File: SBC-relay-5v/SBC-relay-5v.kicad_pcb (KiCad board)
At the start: 2 copper layers, 85 x 56 mm, 52 parts, among them J1 USB_B_Micro, J2 PWR_IN, J3 USB_A_Stacked, J4 USB_A_Stacked, J5 USB_A, J6 USB_A, K1 SANYOU_SRD_Form_A, K2 SANYOU_SRD_Form_A, K3 SANYOU_SRD_Form_A, K4 SANYOU_SRD_Form_A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

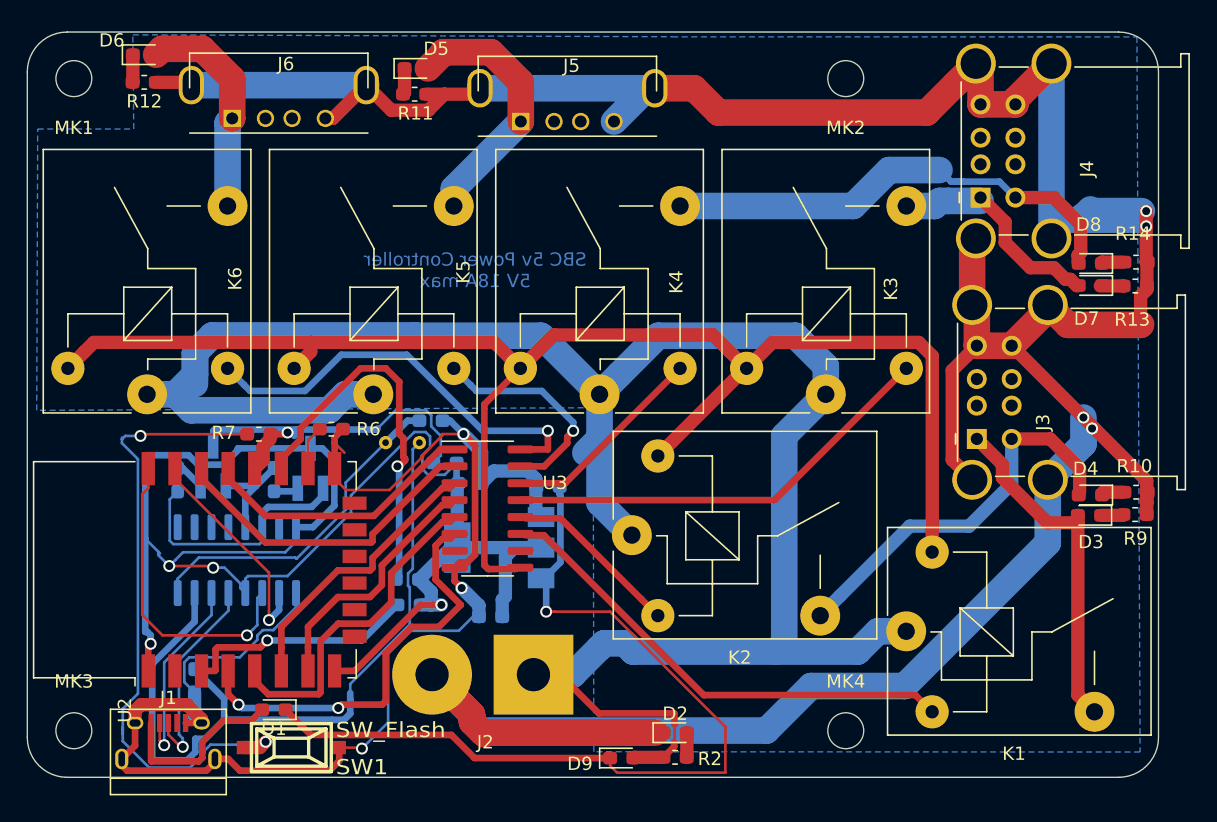
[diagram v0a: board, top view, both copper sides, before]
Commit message: Add modified version of SBC-relay-5v
Signed-off-by: Zamir SUN <sztsian@gmail.com>
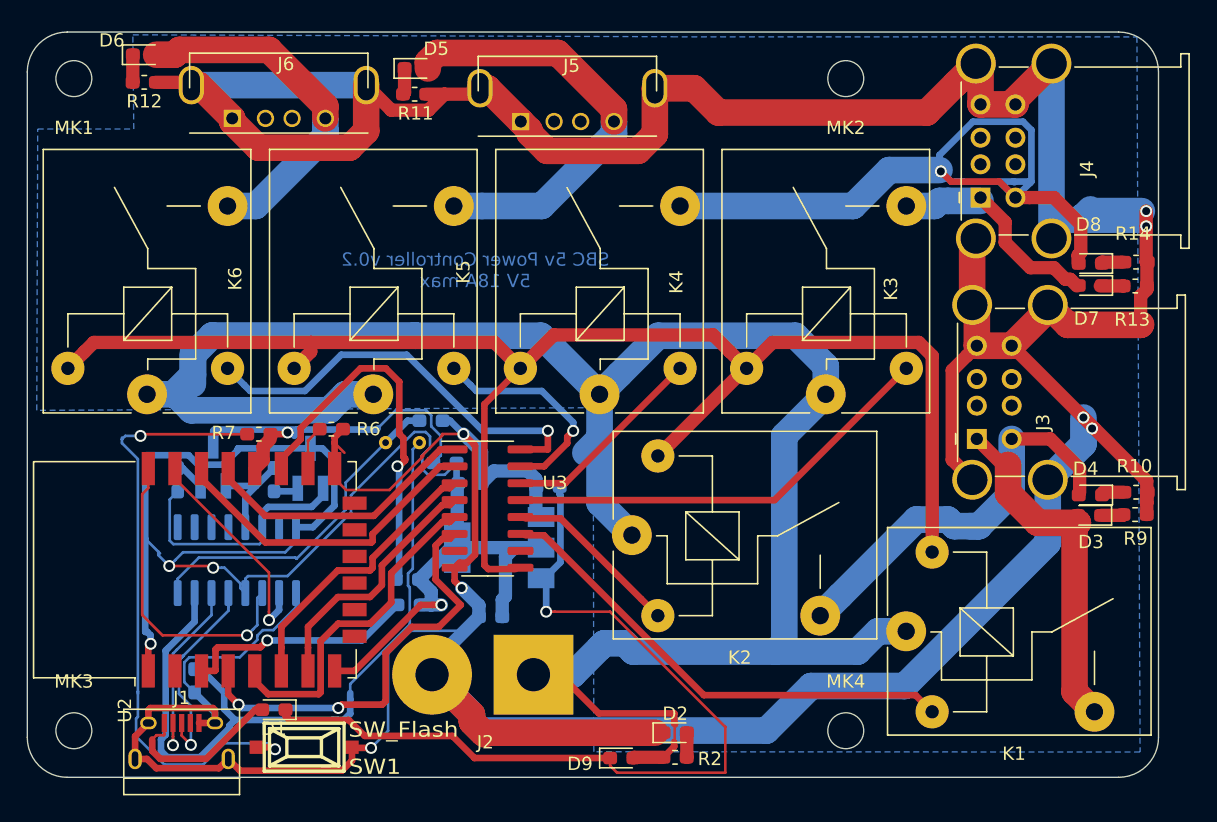
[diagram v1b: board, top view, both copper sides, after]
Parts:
- moved J1 1.00 mm to (211.6, 147.3)
- moved SW1 0.96 mm to (220.8, 147.7)
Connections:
- net GPIO10 renamed Net-(U2-Pad12)
- net GPIO9 renamed Net-(U2-Pad11)
- C1 pad 2: GND -> GND_IN
- C2 pad 2: GND -> GND_IN
- C3 pad 2: GND -> GND_IN
- C4 pad 2: GND -> GND_IN
- C5 pad 2: GND -> GND_IN
- J1 pad 5: GND -> GND_IN
- J1 pad 6: GND -> GND_IN
- R6 pad 1: GND -> GND_IN
- SW1 pad 2: GND -> GND_IN
- U1 pad 1: GND -> GND_IN
- U2 pad 15: GND -> GND_IN
- U3 pad 8: GND -> GND_IN
- U4 pad 1: GND -> GND_IN
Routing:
- net GND_IN: track 263.7 -> 399.3 mm, vias 4 -> 7
- net GND: track 112.8 -> 0.00 mm, vias 3 -> 0
- net Net-(D8-Pad2): track 36.4 -> 60.1 mm, vias 0 -> 1
- net Net-(D4-Pad2): track 29.7 -> 43.1 mm
- net Net-(D5-Pad2): track 20.8 -> 32.6 mm
- net Net-(C4-Pad1): track 69.9 -> 60.0 mm
- net Net-(D6-Pad2): track 16.5 -> 26.4 mm
- net Net-(D3-Pad2): track 26.1 -> 34.6 mm
- net Net-(R7-Pad1): track 48.4 -> 46.4 mm
- net Net-(D1-Pad2): track 13.5 -> 12.8 mm
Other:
- board text added: "SBC 5v Power Controller v0.2 5V 18A max"
- board text removed: "SBC 5v Power Controller 5V 18A max"
